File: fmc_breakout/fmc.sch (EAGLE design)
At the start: 19 parts

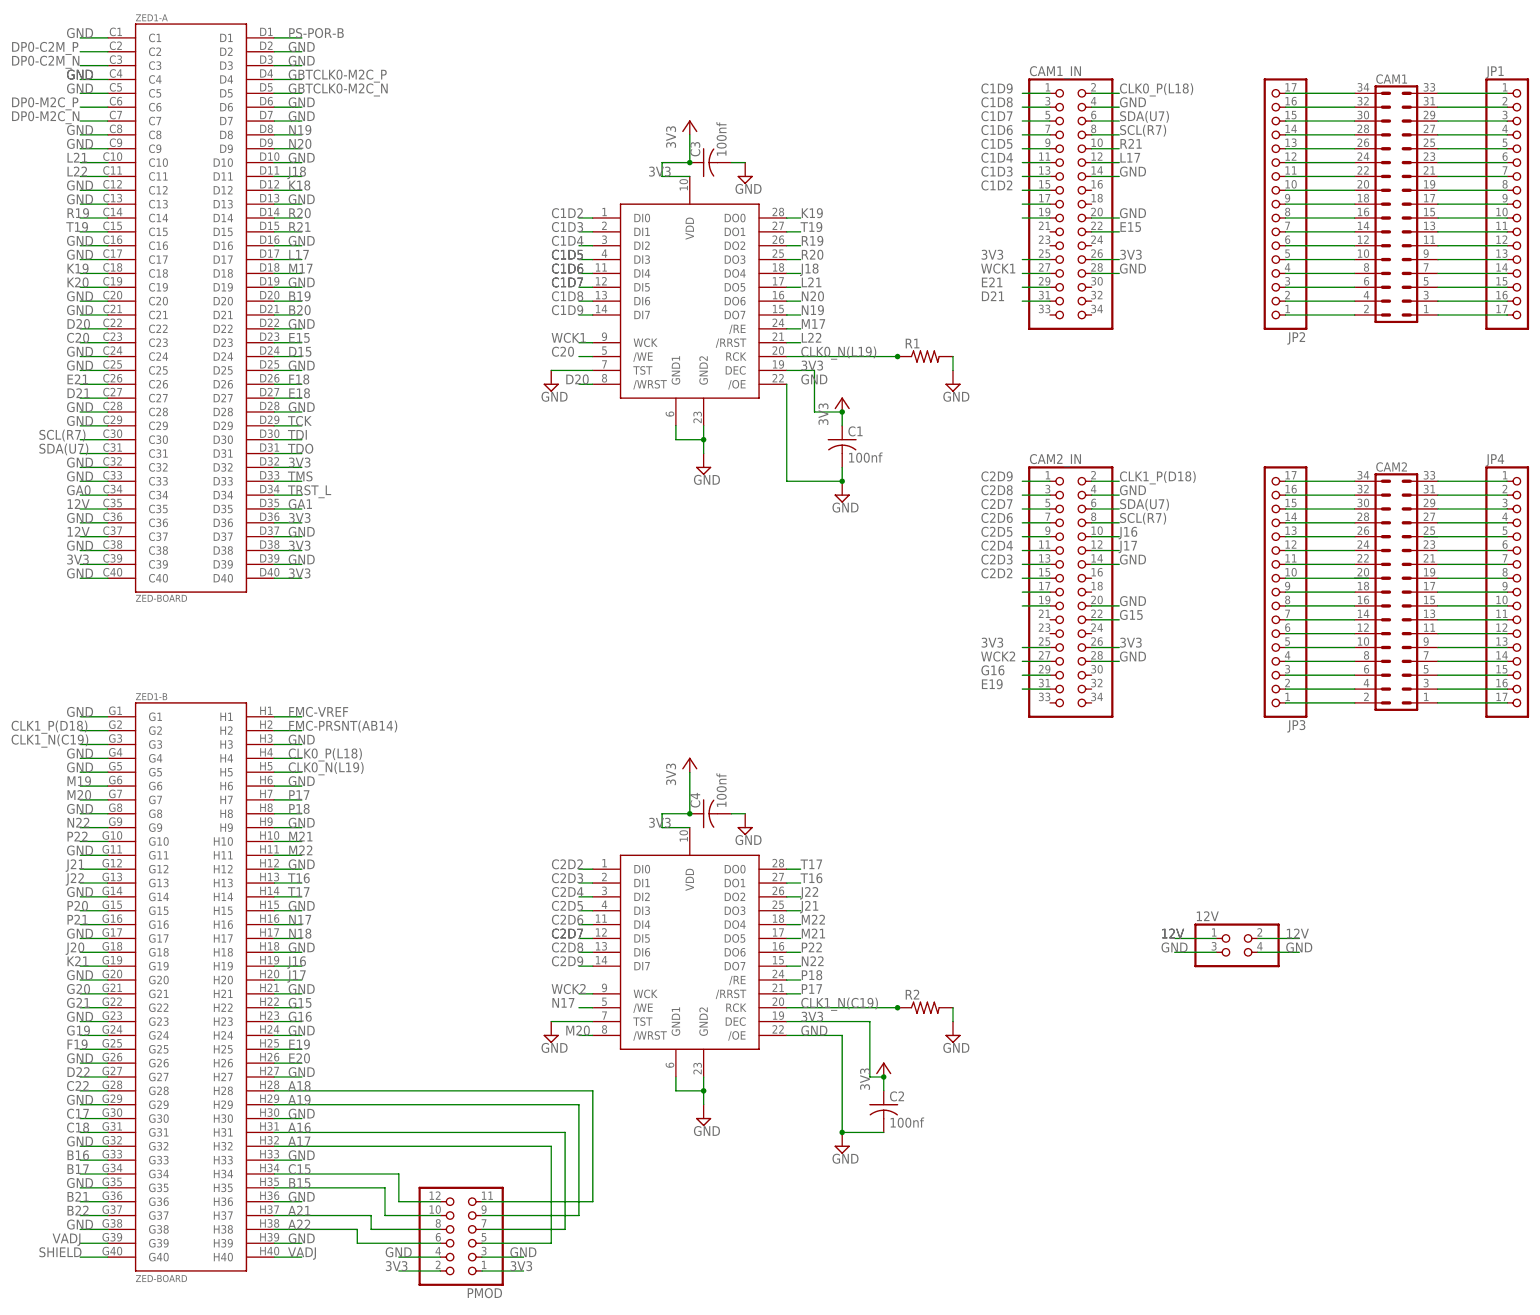
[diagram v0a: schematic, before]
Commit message: Finished routing traces
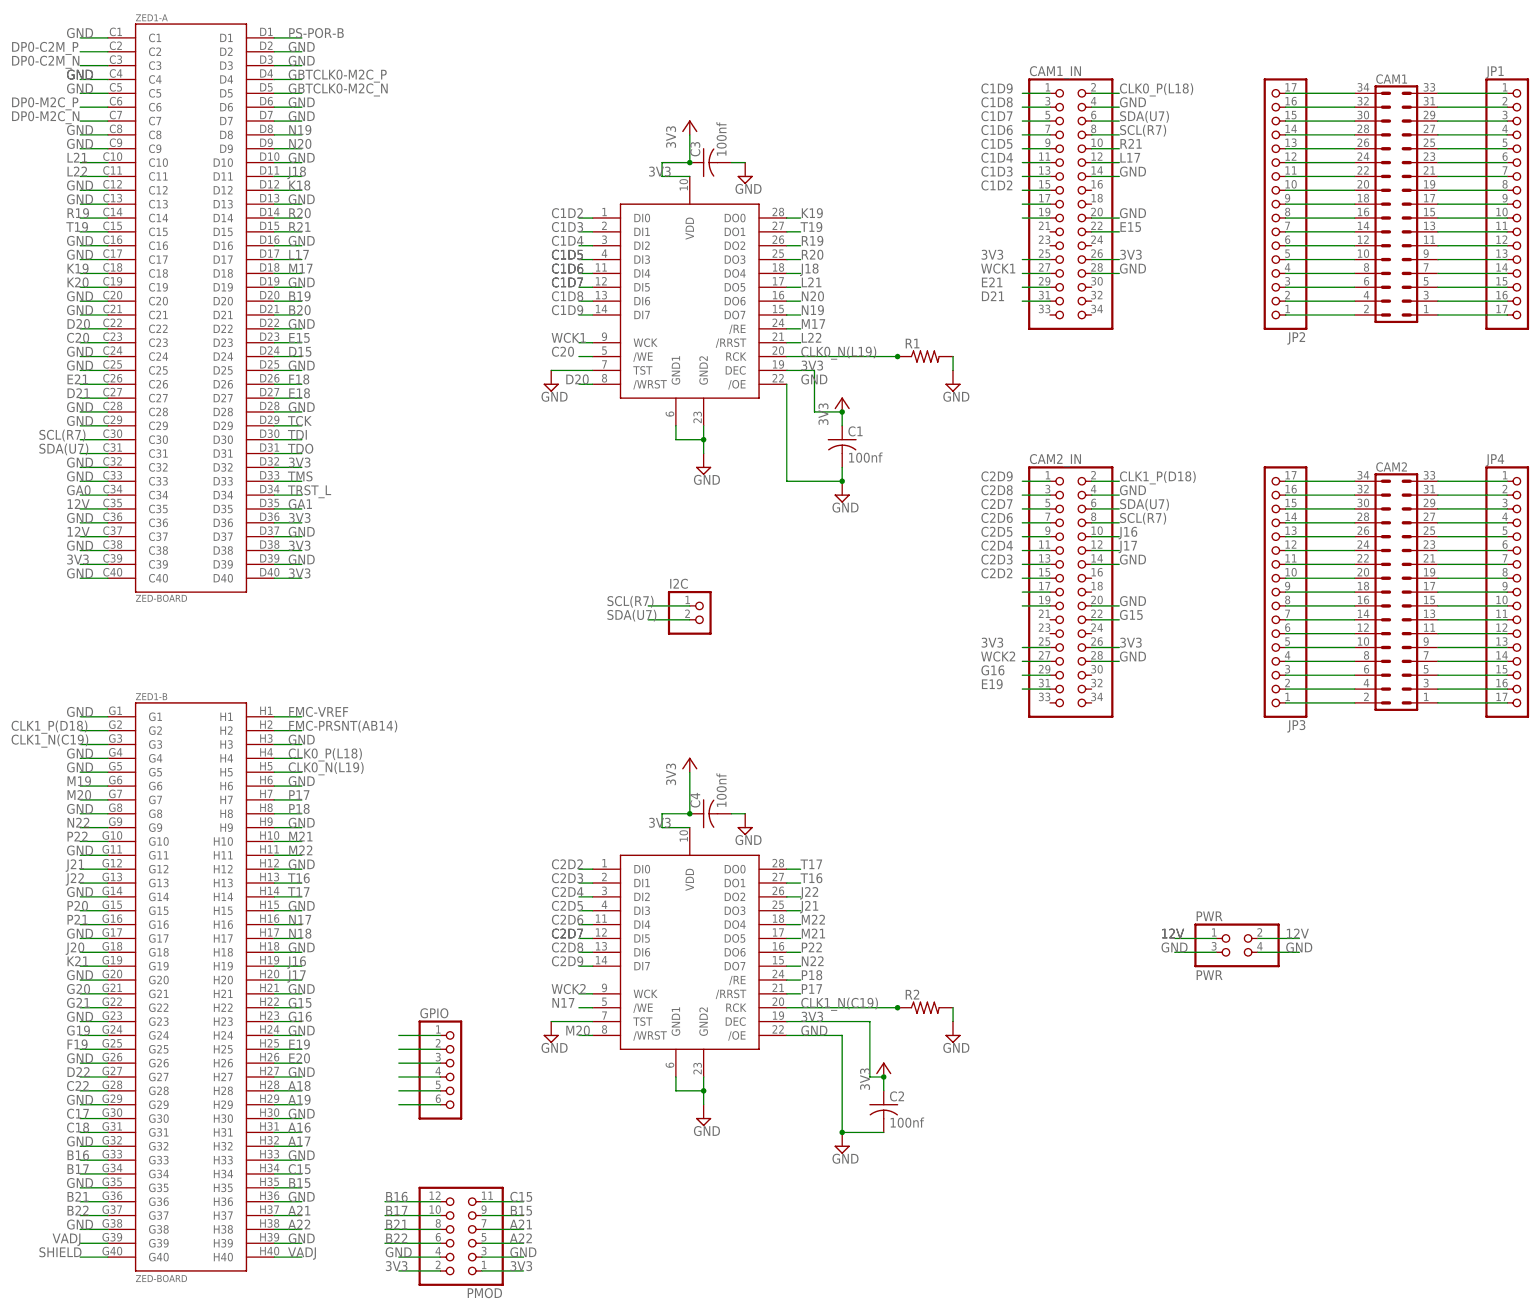
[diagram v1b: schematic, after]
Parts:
- added GPIO: (no value), pinhead:PINHD-1X6
- added I2C: (no value), pinhead:PINHD-1X2
- PWR: value (none) -> PWR
- renumbered 12V to PWR, AL422B to ALA22B_1, U$2 to AL422B_2
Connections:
- net 3V3: now also GPIO.6
- net A16: now also GPIO.3; no longer PMOD.7
- net A17: now also GPIO.4; no longer PMOD.5
- net A18: now also GPIO.1; no longer PMOD.11
- net A19: now also GPIO.2; no longer PMOD.9
- net A21: now also PMOD.7; no longer PMOD.8
- net A22: now also PMOD.5; no longer PMOD.6
- net B15: now also PMOD.9; no longer PMOD.10
- net B16: now also PMOD.12
- net B17: now also PMOD.10
- net B21: now also PMOD.8
- net B22: now also PMOD.6
- net C15: now also PMOD.11; no longer PMOD.12
- net GND: now also GPIO.5
- net N$40: now also CAM2.25
- net N$60: now also CAM2.20
- net SCL(R7): now also I2C.1
- net SDA(U7): now also I2C.2
